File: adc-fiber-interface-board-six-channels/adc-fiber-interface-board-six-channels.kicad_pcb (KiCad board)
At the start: 2 copper layers, 45 x 65.8 mm, 49 parts, among them J1 Conn_02x08_Odd_Even, U1 HFBR-1521Z, U2 HFBR-1521Z, U3 HFBR-1521Z, U4 HFBR-1521Z, U5 HFBR-1521Z, U6 HFBR-1521Z, U7 HFBR-2521Z, U8 HFBR-2521Z, U9 74HCT541

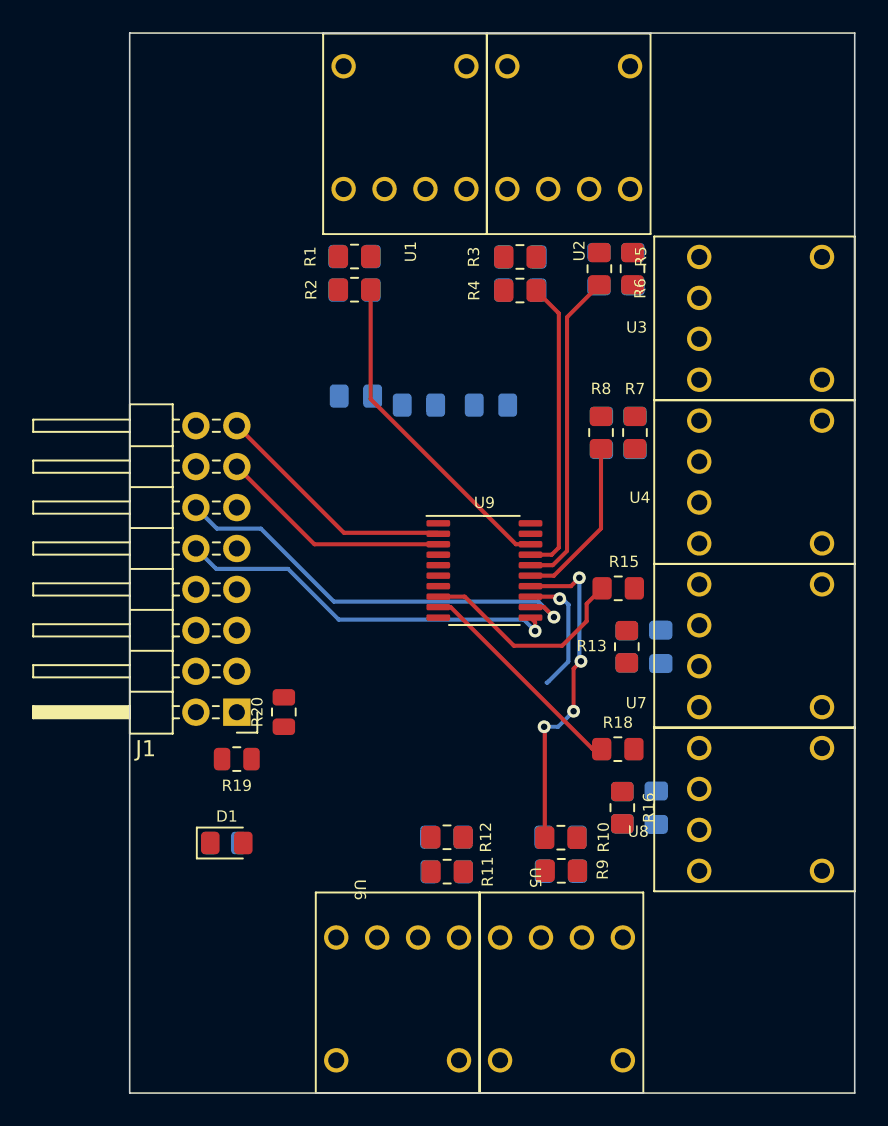
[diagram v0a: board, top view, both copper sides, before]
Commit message: Initial version of adc-fiber board
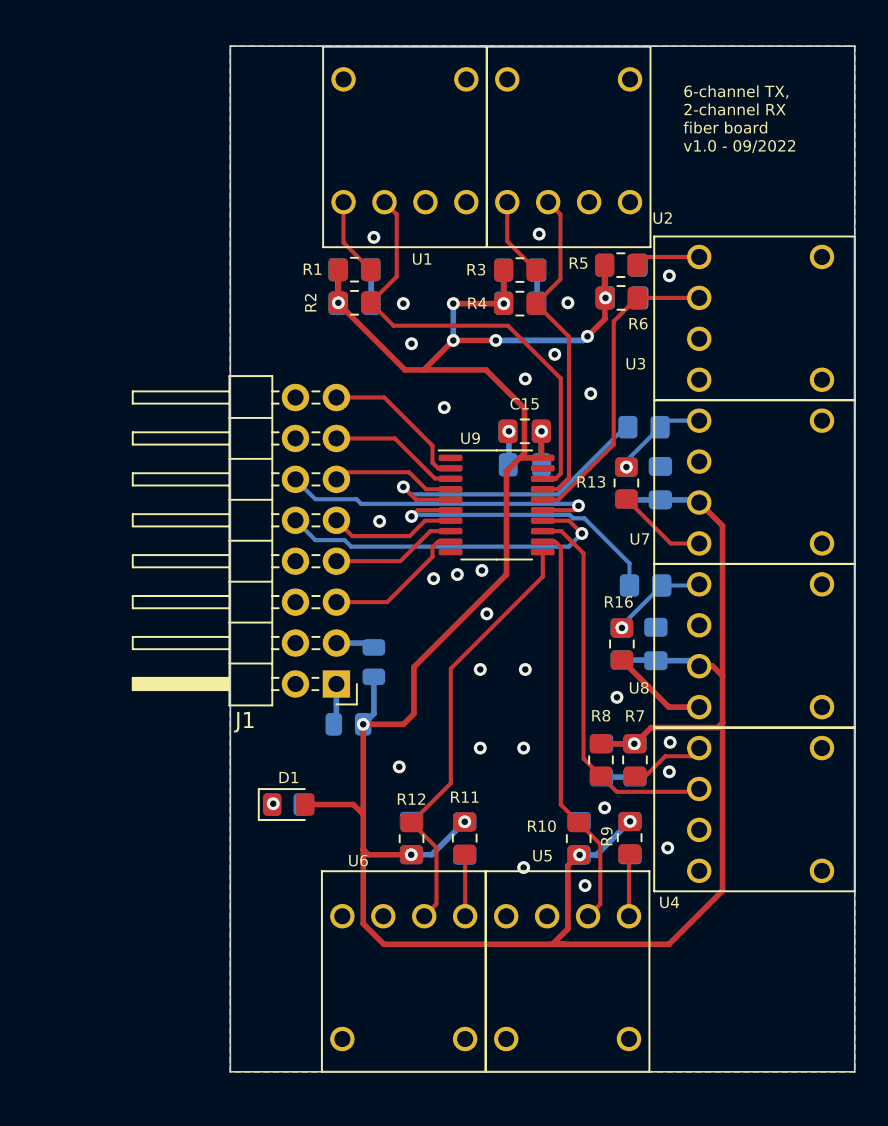
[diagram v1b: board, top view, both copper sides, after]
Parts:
- C15: moved to F.Cu
- R15, R18, R19, R20: moved to B.Cu
- moved C7 20.3 mm to (121.4, 73.9)
- moved C8 20.3 mm to (119.3, 73.9)
- moved R7 20.3 mm to (121.4, 73.8)
- moved R8 20.3 mm to (119.3, 73.8)
- moved U4 20.3 mm to (128.7, 76.9)
- moved C16 11.3 mm to (114.5, 55.5)
- moved R18 10.3 mm to (122.0, 63.0)
- moved C13 10.2 mm to (122.9, 56.7)
- moved C14 10.2 mm to (122.7, 66.6)
- moved R13 10.2 mm to (120.8, 56.7)
- moved R14 10.2 mm to (120.8, 56.7)
- moved R16 10.2 mm to (120.5, 66.6)
- moved R17 10.2 mm to (120.5, 66.6)
- moved U7 10.2 mm to (128.7, 56.6)
- moved U8 10.2 mm to (128.7, 66.8)
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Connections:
- U9 pad 11: /RX2b -> /TX6b
- U9 pad 12: /RX1b -> /TX5b
- U9 pad 13: /TX6b -> /TX4b
- U9 pad 14: /TX5b -> /RX2b
- U9 pad 15: /TX4b -> /RX1b
- U9 pad 5: /TX4 -> /RX1
- U9 pad 6: /TX5 -> /RX2
- U9 pad 7: /TX6 -> /TX4
- U9 pad 8: /RX1 -> /TX5
- U9 pad 9: /RX2 -> /TX6
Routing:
- net VCC: track 0.00 -> 184.3 mm, vias 0 -> 14
- net /TX6b: track 8.00 -> 26.9 mm, vias 1 -> 0
- net /TX4b: track 10.5 -> 23.9 mm
- net /TX6: track 0.00 -> 8.99 mm
- net GND: track 0.00 -> 8.33 mm, vias 0 -> 28
- net /TX4: track 0.00 -> 7.88 mm
- net /TX5: track 0.00 -> 7.86 mm
- net /TX3: track 0.00 -> 7.70 mm
- net /TX1b: track 20.4 -> 28.1 mm
- net /TX2: track 14.5 -> 8.12 mm
- net /RX1b: track 26.8 -> 20.6 mm
- net Net-(R16-Pad1): track 0.00 -> 6.01 mm, vias 0 -> 1
- net Net-(R16-Pad2): track 0.00 -> 6.01 mm
- net Net-(R13-Pad1): track 0.00 -> 5.94 mm, vias 0 -> 1
- net /TX1: track 15.3 -> 9.52 mm
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- added copper zone on B.Cu, net GND
- added copper zone on F.Cu, net GND
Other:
- board size 45 x 65.8 mm -> 38.8 x 63.7 mm
- board text added: "6-channel TX, 2-channel RX fiber board v1.0 - 09/2022"

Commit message: Updated boards with dates, silk, mounting holes
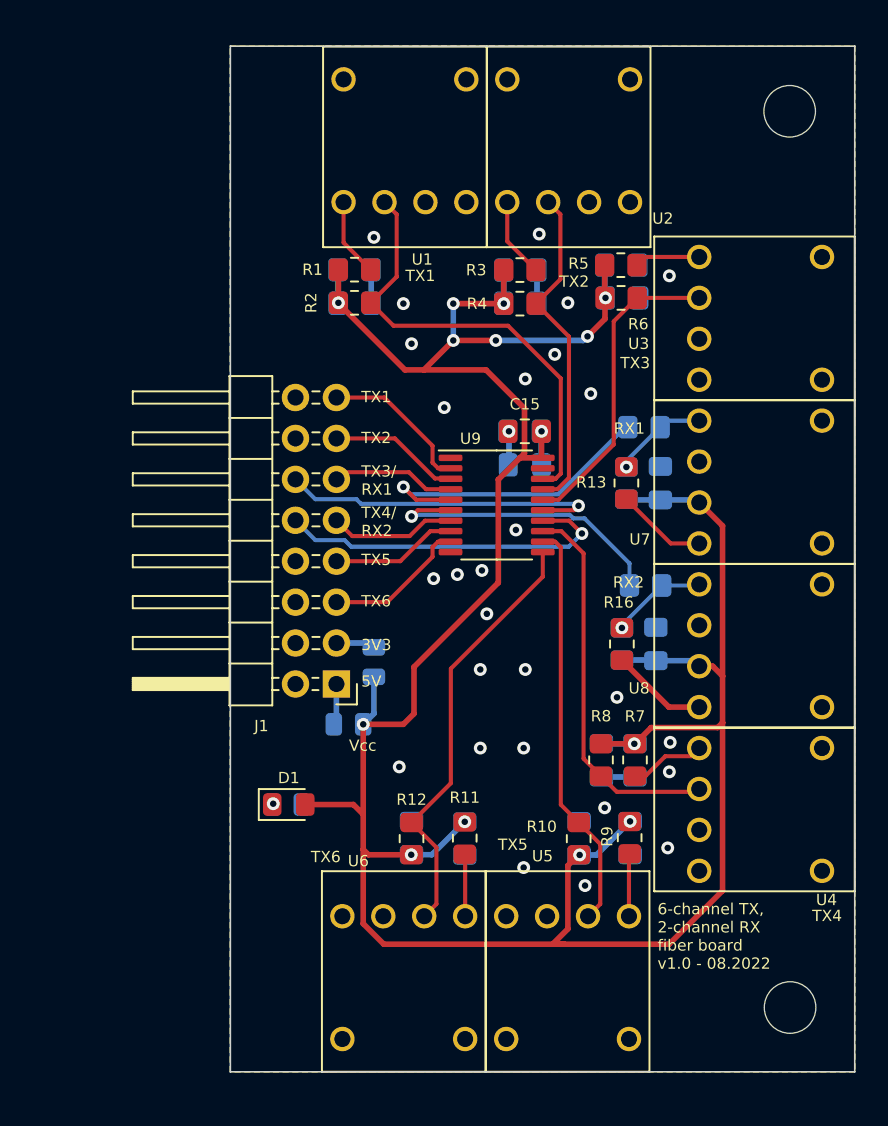
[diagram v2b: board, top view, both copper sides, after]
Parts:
- added REF**: MountingHole_3.2mm_M3, MountingHole:MountingHole_3.2mm_M3, F.Cu at (131.0, 33.6)
- added REF**: MountingHole_3.2mm_M3, MountingHole:MountingHole_3.2mm_M3, F.Cu at (131.0, 89.2)
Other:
- board text added: "3V3"
- board text added: "5V"
- board text added: "6-channel TX, 2-channel RX fiber board v1.0 - 08.2022"
- board text added: "RX1"
- board text added: "RX2"
- board text added: "TX1"
- board text added: "TX2"
- board text added: "TX3"
- board text added: "TX3/ RX1"
- board text added: "TX4"
- board text added: "TX4/ RX2"
- board text added: "TX5"
- board text added: "TX6"
- board text added: "Vcc"
- board text removed: "6-channel TX, 2-channel RX fiber board v1.0 - 09/2022"

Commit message: Finalized optic boards, modified sil in adc-fiber interface board
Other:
- board text added: "Optics board 2 RX/6 TX v1.0 - 08.2022"
- board text removed: "6-channel TX, 2-channel RX fiber board v1.0 - 08.2022"
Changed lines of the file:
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@@
     (effects (font (size 0.7 0.7) (thickness 0.15)) (justify left))
   )
-  (gr_text "6-channel TX,\n2-channel RX \nfiber board\nv1.0 - 08.2022" (at 122.7582 84.7852) (layer "F.SilkS")
+  (gr_text "Optics board\n2 RX/6 TX\nv1.0 - 08.2022" (at 122.936 37.2872) (layer "F.SilkS")
     (effects (font (size 0.7 0.7) (thickness 0.15)) (justify left))
   )
